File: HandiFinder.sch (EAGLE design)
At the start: 25 parts, among them IC2 4047D, X1 SMA-142-0701-801/806

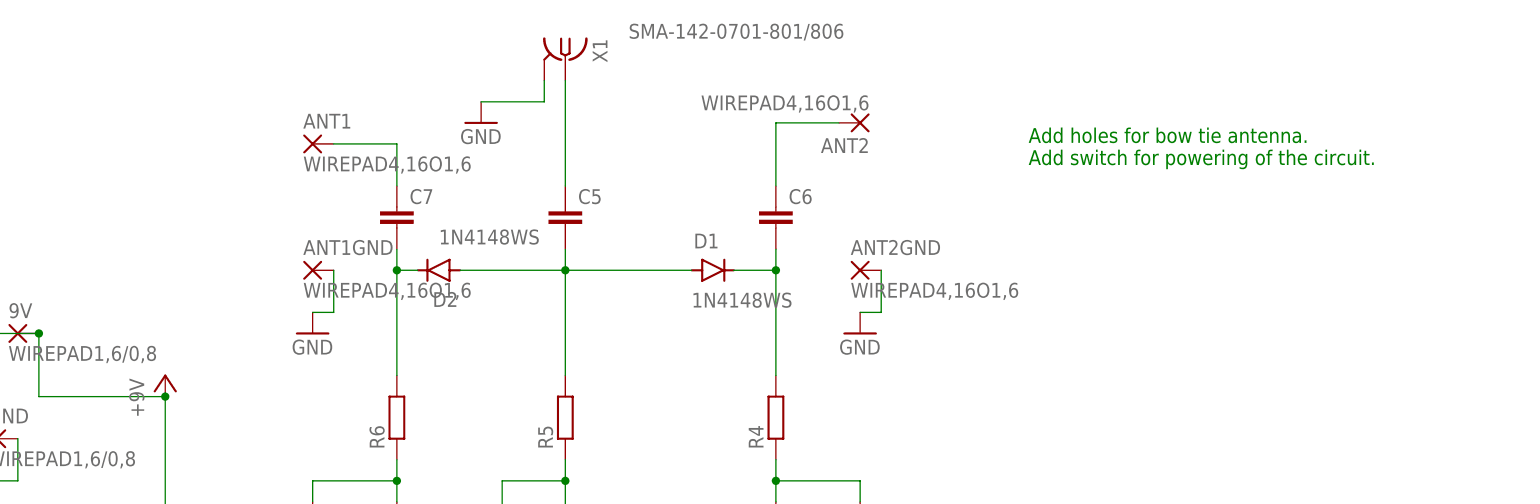
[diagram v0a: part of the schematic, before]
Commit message: Change hole diameter to 2.6mm to allow 2.5mm screw. Change diode footprint to SOD 123.
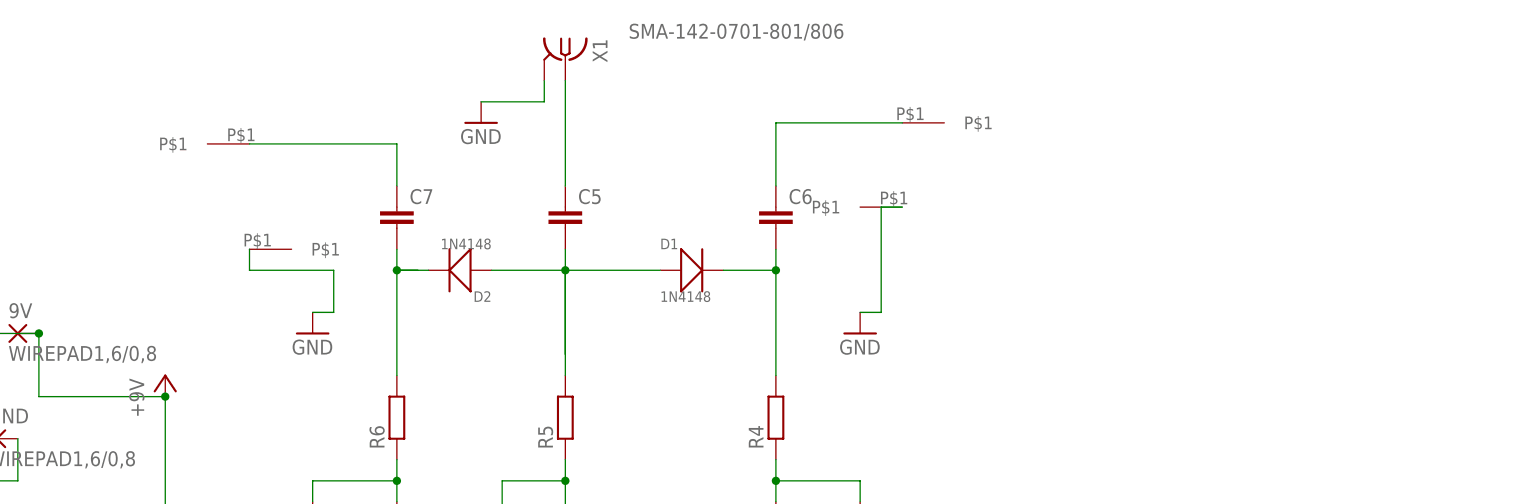
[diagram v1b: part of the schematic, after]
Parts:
- removed ANT1GND, ANT2, ANT2GND: WIREPAD4,16O1,6, wirepad:WIREPAD4,16O1,6
- added ANT1GND2, ANT22, ANT2GND2: WIREPAD, wirepad2.6:WIREPAD
- ANT1: value WIREPAD4,16O1,6 -> ANT12; device wirepad:WIREPAD4,16O1,6 -> wirepad2.6:WIREPAD
- D1, D2: value 1N4148WS -> 1N4148; device Diodes:1N4148WS -> Seeed-Diode-2016:SMD-DIODE-100V-200MA(SOD-123)
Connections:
- net GND: now also ANT1GND2.P$1, ANT2GND2.P$1; no longer ANT1GND.P, ANT2GND.P
- net N$10: now also D1.+, D2.+; no longer D1.A, D2.A
- net N$11: now also D1.-; no longer D1.C
- net N$14: now also ANT1.P$1; no longer ANT1.P
- net N$15: now also ANT22.P$1; no longer ANT2.P
- net N$4: now also D2.-; no longer D2.C
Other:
- note removed: "Add holes for bow tie antenna. Add switch for powering of the circuit."
